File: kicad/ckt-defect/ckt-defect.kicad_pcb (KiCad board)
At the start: 2 copper layers, 99.1 x 61 mm, 90 parts, among them J1 Screw_Terminal_01x02, J10 Micro_SD_Card_Det_Hirose_DM3AT, J11 690-005-299-043, J12 SM04B-SRSS, J13 Conn_01x03, J14 Conn_01x03, J2 SM04B-SRSS, J3 SM04B-SRSS, J4 SM04B-SRSS, J5 SM04B-SRSS, J6 SM04B-SRSS, J7 SM04B-SRSS, J8 SM04B-SRSS, J9 Screw_Terminal_01x02, SW5 FSM4JSMA, SW6 FSM4JSMA, U1 MAX98357AETE+T, U2 AP63205WU, U3 TMP1075D, U4 AZ1117-3.3, U5 ESP32-S2-SOLO, U6 74LVC14, U7 TLP241A

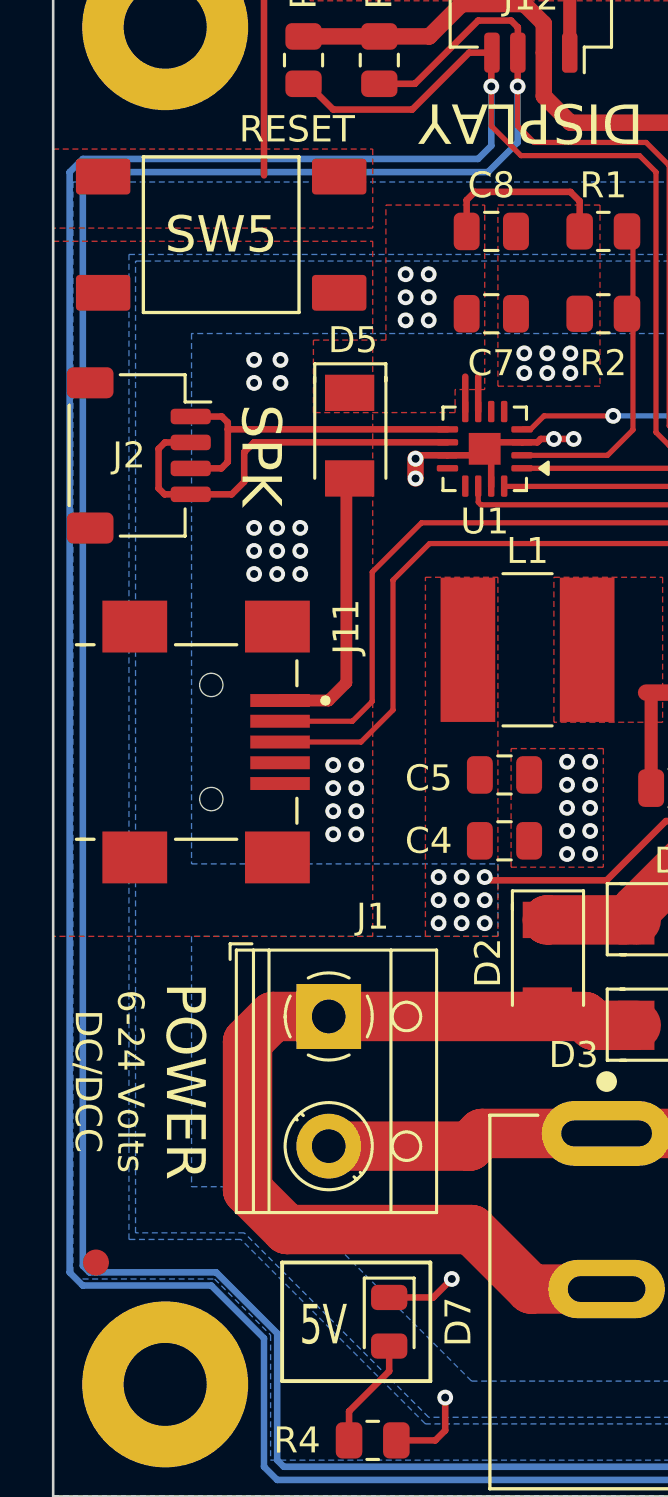
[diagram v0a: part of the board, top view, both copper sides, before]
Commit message: Update tabs to get away from overhangs and delicate stuff
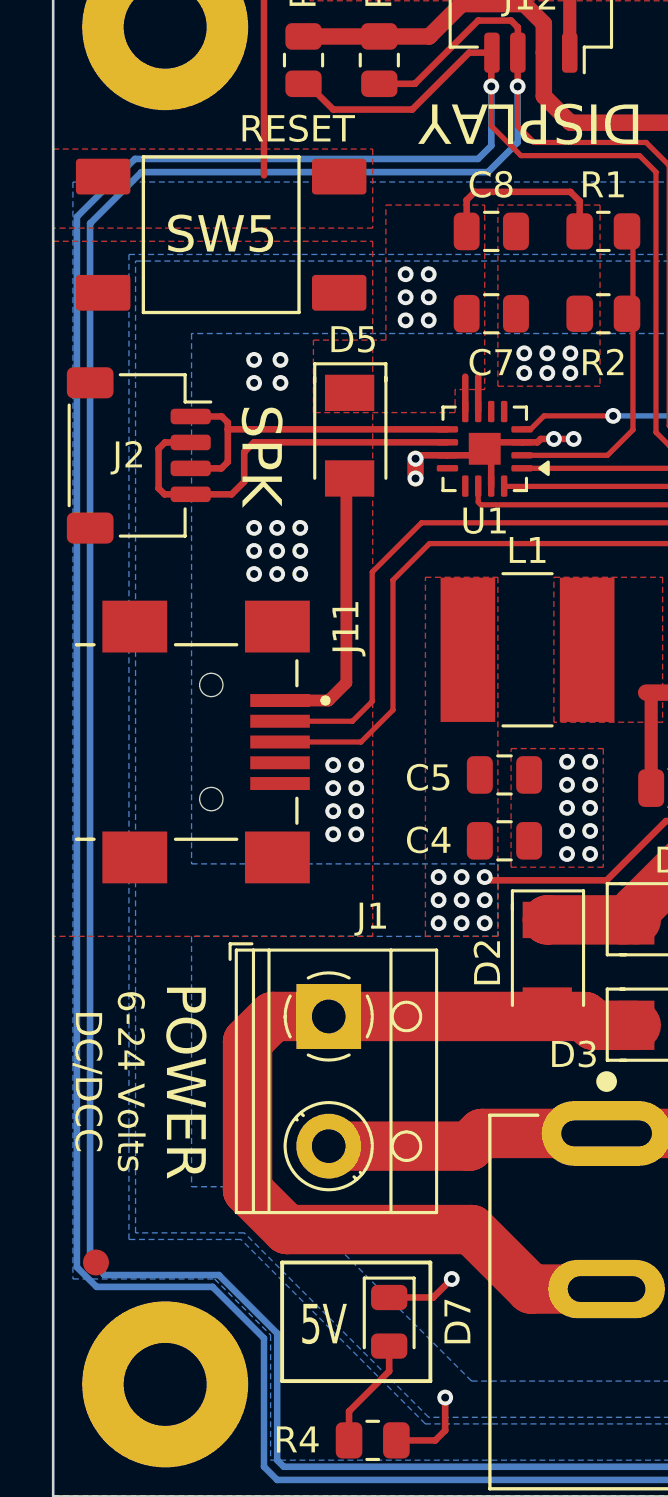
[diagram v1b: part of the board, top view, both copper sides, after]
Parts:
- added REF**: Tab, Kikit:Tab, F.Cu at (55.3, 111.8)
- added REF**: Tab, Kikit:Tab, F.Cu at (145.5, 50.8)
- added REF**: Tab, Kikit:Tab, F.Cu at (145.6, 111.8)
- added REF**: Tab, Kikit:Tab, F.Cu at (50.8, 63.1)
- added REF**: Tab, Kikit:Tab, F.Cu at (55.2, 50.8)
- added REF**: Tab, Kikit:Tab, F.Cu at (149.9, 81.9)
- added REF**: Tab, Kikit:Tab, F.Cu at (50.8, 96.2)
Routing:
- net /SCL: track 223.5 -> 221.8 mm
- net /SDA: track 219.9 -> 218.3 mm
